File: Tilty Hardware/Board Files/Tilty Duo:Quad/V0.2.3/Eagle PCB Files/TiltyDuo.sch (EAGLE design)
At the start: 44 parts, among them U1 TEENSY_3.0_OUTER-PINS28-DIP_S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, U2 HC-09_BREAKOUT, U3 MPL3115A2LGA8, U4 LM2931, U5 MPU-6050, U6 HMC5883LSMD, U7 SPI_FLASH-X25XXSMD

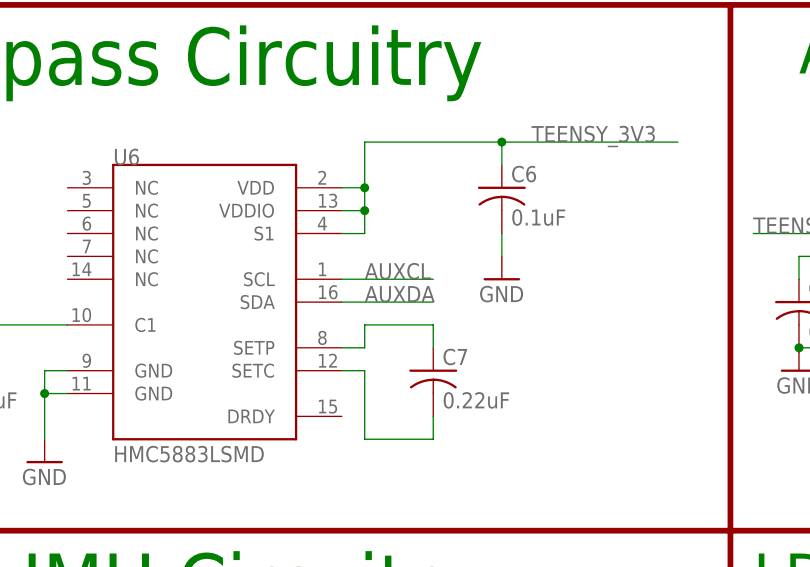
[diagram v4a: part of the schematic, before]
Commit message: Updated Tilty Duo/Quad prototype so compass is no longer on Aux I2C bus
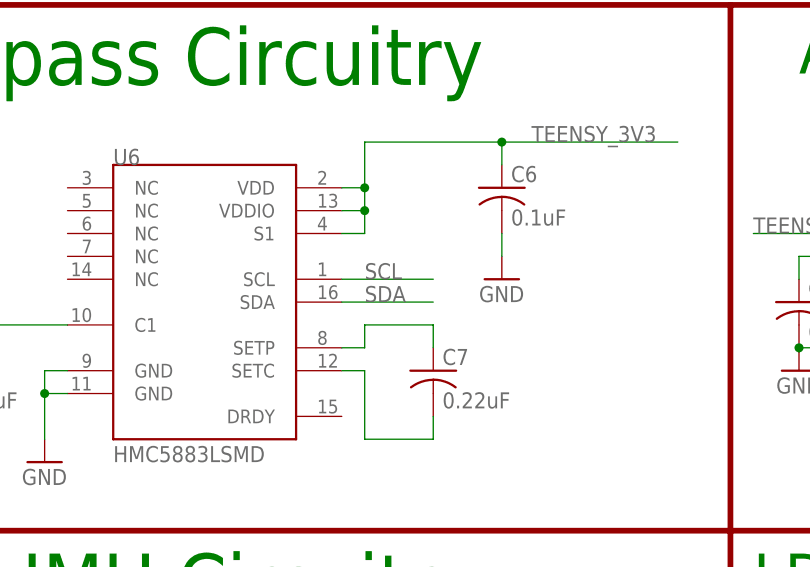
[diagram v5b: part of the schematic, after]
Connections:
- net AUXCL: no longer U6.SCL
- net AUXDA: no longer U6.SDA
- net SCL: now also U6.SCL
- net SDA: now also U6.SDA
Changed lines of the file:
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@@
 <label x="167.64" y="167.64" size="1.778" layer="95"/>
+</segment>
+<segment>
+<wire x1="68.58" y1="162.56" x2="78.74" y2="162.56" width="0.1524" layer="91"/>
+<label x="71.12" y="162.56" size="1.778" layer="95"/>
+<pinref part="U6" gate="G$1" pin="SCL"/>
 </segment>
 </net>
@@
 <wire x1="165.1" y1="165.1" x2="172.72" y2="165.1" width="0.1524" layer="91"/>
 <label x="167.64" y="165.1" size="1.778" layer="95"/>
+</segment>
+<segment>
+<wire x1="68.58" y1="160.02" x2="78.74" y2="160.02" width="0.1524" layer="91"/>
+<label x="71.12" y="160.02" size="1.778" layer="95"/>
+<pinref part="U6" gate="G$1" pin="SDA"/>
 </segment>
 </net>
@@
 </segment>
 <segment>
-<wire x1="68.58" y1="162.56" x2="78.74" y2="162.56" width="0.1524" layer="91"/>
-<label x="71.12" y="162.56" size="1.778" layer="95"/>
-<pinref part="U6" gate="G$1" pin="SCL"/>
-</segment>
-<segment>
 <pinref part="JP6" gate="A" pin="2"/>
 <wire x1="233.68" y1="22.86" x2="227.33" y2="22.86" width="0.1524" layer="91"/>
@@
 </segment>
 <segment>
-<wire x1="68.58" y1="160.02" x2="78.74" y2="160.02" width="0.1524" layer="91"/>
-<label x="71.12" y="160.02" size="1.778" layer="95"/>
-<pinref part="U6" gate="G$1" pin="SDA"/>
-</segment>
-<segment>

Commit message: Lots of little tweaks to perfect the Tilty Duo/Quad and updated ToDo list
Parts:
- added SJ4: SOLDERJUMPERTRACE, SparkFun-Passives:SOLDERJUMPERTRACE
- JP8: device pinhead:PINHD-1X21X02_NO_SILK -> SparkFun-Passives:JUMPER-2SMD-NC
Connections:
- new net N$9: R5.1, SJ4.2
- net GND: now also U1.AGND
- net VBATT: now also SJ4.1; no longer R5.1
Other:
- moved on the sheet: R5, R6

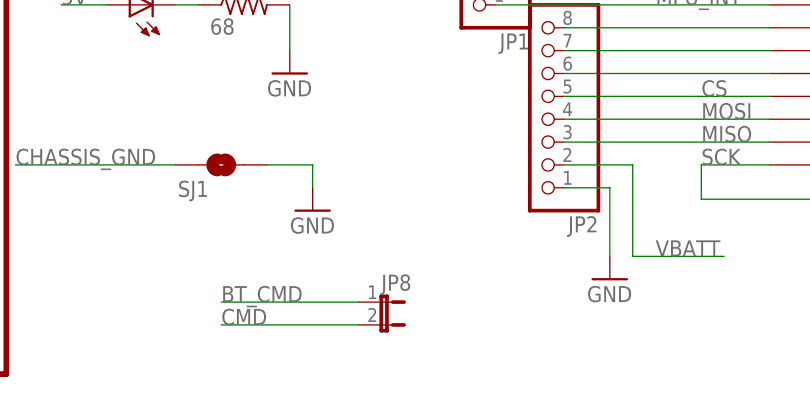
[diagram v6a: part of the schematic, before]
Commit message: Slightly updated Tilty Duo/Quad PCB and added new prototype
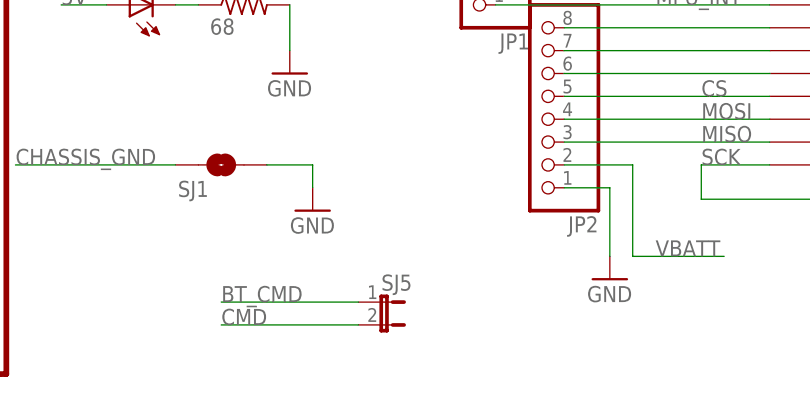
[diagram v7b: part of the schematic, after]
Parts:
- JP4: PART# (none) -> 277-2337-1-ND; POSSIBLE_ALT (none) -> 009276002021106
- U1: PART# (none) -> AE10004-ND; PART#2 (none) -> A28-LC-TR-R
- U7: PART# S25FL204K0TMFI011 -> S25FL204K0TMFI043; PART#2 S25FL208K0RMFI011 -> (none)
- renumbered JP8 to SJ5
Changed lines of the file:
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@@
 <grid distance="0.1" unitdist="inch" unit="inch" style="lines" multiple="1" display="no" altdistance="0.01" altunitdist="inch" altunit="inch"/>
 <layers>
-<layer number="1" name="Top" color="4" fill="1" visible="yes" active="no"/>
-<layer number="16" name="Bottom" color="1" fill="1" visible="yes" active="no"/>
-<layer number="17" name="Pads" color="2" fill="1" visible="yes" active="no"/>
-<layer number="18" name="Vias" color="2" fill="1" visible="yes" active="no"/>
-<layer number="19" name="Unrouted" color="6" fill="1" visible="yes" active="no"/>
-<layer number="20" name="Dimension" color="15" fill="1" visible="yes" active="no"/>
-<layer number="21" name="tPlace" color="16" fill="1" visible="yes" active="no"/>
-<layer number="22" name="bPlace" color="14" fill="1" visible="yes" active="no"/>
-<layer number="23" name="tOrigins" color="15" fill="1" visible="yes" active="no"/>
-<layer number="24" name="bOrigins" color="15" fill="1" visible="yes" active="no"/>
-<layer number="25" name="tNames" color="14" fill="1" visible="yes" active="no"/>
-<layer number="26" name="bNames" color="6" fill="1" visible="yes" active="no"/>
-<layer number="27" name="tValues" color="7" fill="1" visible="yes" active="no"/>
-<layer number="28" name="bValues" color="7" fill="1" visible="yes" active="no"/>
+<layer number="1" name="Top" color="4" fill="1" visible="no" active="no"/>
+<layer number="16" name="Bottom" color="1" fill="1" visible="no" active="no"/>
+<layer number="17" name="Pads" color="2" fill="1" visible="no" active="no"/>
+<layer number="18" name="Vias" color="2" fill="1" visible="no" active="no"/>
+<layer number="19" name="Unrouted" color="6" fill="1" visible="no" active="no"/>
+<layer number="20" name="Dimension" color="15" fill="1" visible="no" active="no"/>
+<layer number="21" name="tPlace" color="16" fill="1" visible="no" active="no"/>
+<layer number="22" name="bPlace" color="14" fill="1" visible="no" active="no"/>
+<layer number="23" name="tOrigins" color="15" fill="1" visible="no" active="no"/>
+<layer number="24" name="bOrigins" color="15" fill="1" visible="no" active="no"/>
+<layer number="25" name="tNames" color="14" fill="1" visible="no" active="no"/>
+<layer number="26" name="bNames" color="6" fill="1" visible="no" active="no"/>
+<layer number="27" name="tValues" color="7" fill="1" visible="no" active="no"/>
+<layer number="28" name="bValues" color="7" fill="1" visible="no" active="no"/>
 <layer number="29" name="tStop" color="7" fill="3" visible="no" active="no"/>
 <layer number="30" name="bStop" color="7" fill="6" visible="no" active="no"/>
@@
 <layer number="35" name="tGlue" color="7" fill="4" visible="no" active="no"/>
 <layer number="36" name="bGlue" color="7" fill="5" visible="no" active="no"/>
-<layer number="37" name="tTest" color="7" fill="1" visible="yes" active="no"/>
-<layer number="38" name="bTest" color="7" fill="1" visible="yes" active="no"/>
+<layer number="37" name="tTest" color="7" fill="1" visible="no" active="no"/>
+<layer number="38" name="bTest" color="7" fill="1" visible="no" active="no"/>
 <layer number="39" name="tKeepout" color="4" fill="11" visible="no" active="no"/>
 <layer number="40" name="bKeepout" color="1" fill="11" visible="no" active="no"/>
@@
 <layer number="44" name="Drills" color="7" fill="1" visible="no" active="no"/>
 <layer number="45" name="Holes" color="7" fill="1" visible="no" active="no"/>
-<layer number="46" name="Milling" color="3" fill="1" visible="yes" active="no"/>
-<layer number="47" name="Measures" color="7" fill="1" visible="yes" active="no"/>
-<layer number="48" name="Document" color="7" fill="1" visible="yes" active="no"/>
-<layer number="49" name="Reference" color="7" fill="1" visible="yes" active="no"/>
-<layer number="50" name="dxf" color="7" fill="1" visible="yes" active="no"/>
-<layer number="51" name="tDocu" color="6" fill="1" visible="yes" active="no"/>
-<layer number="52" name="bDocu" color="7" fill="1" visible="yes" active="no"/>
-<layer number="53" name="tGND_GNDA" color="7" fill="9" visible="yes" active="no"/>
-<layer number="54" name="bGND_GNDA" color="1" fill="9" visible="yes" active="no"/>
-<layer number="56" name="wert" color="7" fill="1" visible="yes" active="no"/>
+<layer number="46" name="Milling" color="3" fill="1" visible="no" active="no"/>
+<layer number="47" name="Measures" color="7" fill="1" visible="no" active="no"/>
+<layer number="48" name="Document" color="7" fill="1" visible="no" active="no"/>
+<layer number="49" name="Reference" color="7" fill="1" visible="no" active="no"/>
+<layer number="50" name="dxf" color="7" fill="1" visible="no" active="no"/>
+<layer number="51" name="tDocu" color="6" fill="1" visible="no" active="no"/>
+<layer number="52" name="bDocu" color="7" fill="1" visible="no" active="no"/>
+<layer number="53" name="tGND_GNDA" color="7" fill="9" visible="no" active="no"/>
+<layer number="54" name="bGND_GNDA" color="1" fill="9" visible="no" active="no"/>
+<layer number="56" name="wert" color="7" fill="1" visible="no" active="no"/>
 <layer number="91" name="Nets" color="2" fill="1" visible="yes" active="yes"/>
 <layer number="92" name="Busses" color="1" fill="1" visible="yes" active="yes"/>
@@
 <part name="R6" library="resistor" deviceset="R-US_" device="R0603" value="680"/>
 <part name="GND13" library="supply1" deviceset="GND" device=""/>
-<part name="JP4" library="My Parts" deviceset="2-POS_SMD_TERM_BLOCK" device=""/>
+<part name="JP4" library="My Parts" deviceset="2-POS_SMD_TERM_BLOCK" device="">
+<attribute name="PART#" value="277-2337-1-ND"/>
+<attribute name="POSSIBLE_ALT" value="009276002021106"/>
+</part>
 <part name="U4" library="on-semiconductor" deviceset="LM2931" device="">
 <attribute name="COST" value="0.53"/>
@@
 <part name="U1" library="My Parts" deviceset="TEENSY_3.0_OUTER-PINS" device="28-DIP_SOCKET">
 <attribute name="COST" value="0.28"/>
+<attribute name="PART#" value="AE10004-ND"/>
+<attribute name="PART#2" value="A28-LC-TR-R"/>
 </part>
 <part name="JP1" library="pinhead" deviceset="PINHD-1X8" device="1X08_NO_SILK_LOCK"/>
@@
 <part name="GND25" library="SparkFun" deviceset="GND" device=""/>
 <part name="U7" library="SparkFun-DigitalIC" deviceset="SPI_FLASH-X25XX" device="SMD">
-<attribute name="PART#" value="S25FL204K0TMFI011"/>
-<attribute name="PART#2" value="S25FL208K0RMFI011"/>
+<attribute name="PART#" value="S25FL204K0TMFI043"/>
 </part>
 <part name="C13" library="resistor" deviceset="C-US" device="C0603" value="0.1uF">
@@
 <part name="R4" library="resistor" deviceset="R-US_" device="R0603" value="68"/>
 <part name="SJ4" library="SparkFun-Passives" deviceset="SOLDERJUMPER" device="TRACE"/>
-<part name="JP8" library="SparkFun-Passives" deviceset="JUMPER-2" device="SMD-NC"/>
+<part name="SJ5" library="SparkFun-Passives" deviceset="JUMPER-2" device="SMD-NC"/>
 </parts>
 <sheets>
@@
 <instance part="R6" gate="G$1" x="123.19" y="63.5" rot="R90"/>
 <instance part="GND13" gate="1" x="123.19" y="55.88"/>
-<instance part="JP4" gate="G$1" x="200.025" y="104.775"/>
+<instance part="JP4" gate="G$1" x="200.025" y="104.775">
+<attribute name="PART#" x="200.025" y="104.775" size="1.778" layer="96" display="off"/>
+<attribute name="POSSIBLE_ALT" x="200.025" y="104.775" size="1.778" layer="96" display="off"/>
+</instance>
 <instance part="U4" gate="G$1" x="142.24" y="111.76">
 <attribute name="COST" x="142.24" y="111.76" size="3.81" layer="96" ratio="14" display="off"/>
@@
 <attribute name="NAME" x="184.912" y="64.77" size="1.27" layer="95" font="vector" ratio="15"/>
 <attribute name="COST" x="187.96" y="45.72" size="3.81" layer="96" ratio="14" display="off"/>
+<attribute name="PART#" x="187.96" y="45.72" size="1.778" layer="96" display="off"/>
+<attribute name="PART#2" x="187.96" y="45.72" size="1.778" layer="96" display="off"/>
 </instance>
 <instance part="JP1" gate="A" x="139.7" y="53.34" rot="R180"/>
@@
 <instance part="U7" gate="G$1" x="218.44" y="165.1">
 <attribute name="PART#" x="218.44" y="165.1" size="1.778" layer="96" display="off"/>
-<attribute name="PART#2" x="218.44" y="165.1" size="1.778" layer="96" display="off"/>
 </instance>
 <instance part="C13" gate="G$1" x="195.58" y="175.26" rot="R90">
@@
 <attribute name="NAME" x="105.41" y="71.12" size="1.778" layer="95"/>
 </instance>
-<instance part="JP8" gate="A" x="129.54" y="10.16" rot="R270"/>
+<instance part="SJ5" gate="A" x="129.54" y="10.16" rot="R270"/>
 </instances>
 <busses>
@@
 <wire x1="127" y1="7.62" x2="111.76" y2="7.62" width="0.1524" layer="91"/>
 <label x="111.76" y="7.62" size="1.778" layer="95"/>
-<pinref part="JP8" gate="A" pin="2"/>
+<pinref part="SJ5" gate="A" pin="2"/>
 </segment>
 </net>
@@
 <wire x1="127" y1="10.16" x2="111.76" y2="10.16" width="0.1524" layer="91"/>
 <label x="111.76" y="10.16" size="1.778" layer="95"/>
-<pinref part="JP8" gate="A" pin="1"/>
-</segment>
-<segment>
+<pinref part="SJ5" gate="A" pin="1"/>
+</segment>
+<segment>
